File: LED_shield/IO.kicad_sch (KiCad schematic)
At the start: 69 parts, among them J201 Raspberry_Pi_2_3, Q201 PMOS, Q202 NMOS, Q203 NMOS, Q204 NMOS, Q205 NMOS, SW201 SW_DIP_x08, SW202 SW_DIP_x08, U201 7414, U202 7414, U203 4052

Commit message: Finish most of PCB design
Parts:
- added C204, C205, C206: 100n, Capacitor_SMD:C_0402_1005Metric, symbol Device:C
- R201, R202, R203: footprint Resistor_SMD:R_0603_1608Metric -> Resistor_SMD:R_0402_1005Metric; LCSC (none) -> C11702
- R204: renamed from R209; LCSC (none) -> C22797
- R205: renamed from R210; footprint Resistor_SMD:R_0603_1608Metric -> Resistor_SMD:R_0402_1005Metric; LCSC (none) -> C11702
- R206: renamed from R211; footprint Resistor_SMD:R_0603_1608Metric -> Resistor_SMD:R_0402_1005Metric; LCSC (none) -> C11702
- R207: renamed from R212; footprint Resistor_SMD:R_0603_1608Metric -> Resistor_SMD:R_0402_1005Metric; LCSC (none) -> C11702
- R209: renamed from R213; footprint Resistor_SMD:R_0603_1608Metric -> Resistor_SMD:R_0402_1005Metric; LCSC (none) -> C11702
- R210: renamed from R214; footprint Resistor_SMD:R_0603_1608Metric -> Resistor_SMD:R_0402_1005Metric; LCSC (none) -> C11702
- R211: renamed from R206; footprint Resistor_SMD:R_0603_1608Metric -> Resistor_SMD:R_0402_1005Metric; LCSC (none) -> C25744
- R212: renamed from R205; footprint Resistor_SMD:R_0603_1608Metric -> Resistor_SMD:R_0402_1005Metric; LCSC (none) -> C25744
- R213: renamed from R207; footprint Resistor_SMD:R_0603_1608Metric -> Resistor_SMD:R_0402_1005Metric; LCSC (none) -> C25744
- R214: renamed from R208; footprint Resistor_SMD:R_0603_1608Metric -> Resistor_SMD:R_0402_1005Metric; LCSC (none) -> C25744
- renumbered R204 to R208, R223 to R218, R221 to R219, R222 to R220, R224 to R221, R225 to R222, R227 to R223, R228 to R224, R226 to R225, R218 to R226, R219 to R227, R220 to R228, R235 to R232, R232 to R233, R233 to R234, R234 to R235, U203 to U201, U201 to U203
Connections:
- net +5V: now also C204.1, C205.1
- net 3V3: now also C206.1
- net ADC_{0}MCU: now also C201.1, R204.2, R205.1, U201.12 (X0)
- net ADC_{1}MCU: now also C203.1, R209.2, R210.1, U201.14 (X1)
- net GND: now also C204.2, C205.2, C206.2
- net LED0_MCU: now also A202.20 (GPIO15), U202.5; no longer A202.1 (GPIO0), U202.1
- net LED1_MCU: now also A202.19 (GPIO14); no longer A202.2 (GPIO1)
- net LED2_MCU: now also A202.15 (GPIO11), U202.1; no longer A202.4 (GPIO2), U202.5
- net LED3_MCU: now also A202.10 (GPIO7), U203.5; no longer A202.5 (GPIO3), U202.9
- net LED4_MCU: now also A202.9 (GPIO6), U203.3; no longer A202.21 (GPIO16), U203.11
- net LED5_MCU: now also A202.7 (GPIO5), U203.1; no longer A202.22 (GPIO17), U203.13
- net LED_OUT_0: now also U202.8; no longer U203.2
- net LED_OUT_1: now also U202.10; no longer U203.4
- net LED_OUT_2: now also U202.12; no longer U203.6
- net LED_OUT_4: now also U203.10; no longer U202.10
- net LED_OUT_5: now also U203.12; no longer U202.12
- net btn_read1: now also A202.21 (GPIO16); no longer A202.15 (GPIO11)
- net btn_read2: now also A202.24 (GPIO18); no longer A202.19 (GPIO14)
- net btn_read3: now also A202.22 (GPIO17); no longer A202.20 (GPIO15)
- net btn_sel0: now also A202.29 (GPIO22); no longer A202.6 (GPIO4)
- net btn_sel1: now also A202.25 (GPIO19); no longer A202.7 (GPIO5)
- net btn_sel2: now also A202.26 (GPIO20); no longer A202.9 (GPIO6)
- net btn_sel3: now also A202.27 (GPIO21); no longer A202.10 (GPIO7)
- net at U202.2: now also U202.13; no longer U203.1
- net at U203.9: now also U203.6; no longer U202.8
- net at U202.11: now also U202.4; no longer U203.10
- net at U202.6: now also U202.9; no longer U203.5
- new net: U203.13, U203.2
- new net: U203.11, U203.4
- no-connect marks 6 -> 42
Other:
- moved on the sheet: U202A, U202C, U202D, U202E, U202F, U203A, U203B, U203C, U203E, U203F

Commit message: Remove unused components
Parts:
- removed A201: Arduino_Nano_ESP32_Socket, PCM_arduino-library:Arduino_Nano_ESP32_Socket, symbol PCM_arduino-library:Arduino_Nano_ESP32_Socket
- removed C202, C206: 100n, Capacitor_SMD:C_0402_1005Metric, symbol Device:C
- removed D201: D_Schottky, symbol Device:D_Schottky
- removed J201: Raspberry_Pi_2_3, Connector_PinSocket_2.54mm:PinSocket_2x17_P2.54mm_Vertical, symbol Connector:Raspberry_Pi_2_3
- removed R201, R206, R207: 1k, Resistor_SMD:R_0402_1005Metric, symbol Device:R_US
- removed R215, R216, R217, R218, R219, R220, R221, R222, R223, R224, R225, R226, R227, R228, R229, R230, R231, R232, R233, R234, R235, R236: 0R, Resistor_SMD:R_0402_1005Metric, symbol Device:R_US
- removed U201: 4052, Package_SO:SO-16_3.9x9.9mm_P1.27mm, symbol 4xxx:4052
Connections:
- net 12VIN renamed VIN
- no-connect marks 42 -> 16
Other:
- note added: "7414 decoupling"
- note added: "MCU module"
- note added: "Output buffering"
- note added: "Voltage dividers for rail monitoring"
- note added: "dip switch matrix"
- moved on the sheet: A202, C201, C203, C204, C205, D202, D203, D204, D205, D206, D207, D208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

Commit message: Small fixes before production
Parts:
- removed D202, D203, D204, D205, D206, D207, D208, D209, D210, D211, D212, D213, D214, D215, D216, D217: D_Small_Filled, Diode_SMD:D_0603_1608Metric, symbol Device:D_Small_Filled
- removed Q202, Q203, Q204, Q205: NMOS, Package_TO_SOT_SMD:SOT-23, symbol Simulation_SPICE:NMOS
- added C202, C206: 100n, Capacitor_SMD:C_0402_1005Metric, symbol Device:C
- added R201, R206, R207, R215, R216, R217, R218, R219, R220, R221, R222, R223: 100k, Resistor_SMD:R_0402_1005Metric, symbol Device:R_US
- added U201, U204: 74HC165, Package_SO:SOIC-16_3.9x9.9mm_P1.27mm, symbol 74xx:74HC165
- Q201: symbol Simulation_SPICE:PMOS -> Device:Q_PMOS_GSD; LCSC (none) -> C10487
- R211, R212, R213, R214: value 10k -> 100k; LCSC C25744 -> C25741
- SW201, SW202: footprint Button_Switch_SMD:SW_DIP_SPSTx08_Slide_6.7x21.88mm_W6.73mm_P2.54mm_LowProfile_JPin -> Button_Switch_SMD:SW_DIP_SPSTx08_Slide_6.7x21.88mm_W8.61mm_P2.54mm_LowProfile
- U202, U203: LCSC (none) -> C5605
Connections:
- net +5V: now also Q201.3 (D); no longer Q201.1 (D)
- net 3V3: now also SW201.10, SW201.11, SW201.12, SW201.13, SW201.14, SW201.15, SW201.16, SW201.9, SW202.1, SW202.2, SW202.3, SW202.4, SW202.5, SW202.6, SW202.7, SW202.8, C202.1, C206.1, U201.16 (VCC), U204.16 (VCC); no longer R211.2, R212.2, R213.2, R214.2
- net 5V_local: now also Q201.2 (S); no longer Q201.3 (S)
- net GND: now also R211.2, R212.2, R213.2, R214.2, C202.2, C206.2, R201.2, R206.2, R207.2, R215.2, R216.2, R217.2, R218.2, R219.2, R220.2, R221.2, R222.2, R223.2, U201.8 (GND), U204.8 (GND)
- net btn_read0: no longer SW201.13, SW201.14, SW201.15, SW201.16
- net at SW201.7: now also R206.1, U204.5 (D6)
- net at R213.1: now also SW201.3, U204.13 (D2)
- net at R211.1: now also SW201.5, U204.3 (D4)
- net at R212.1: now also SW201.4, U204.14 (D3)
- net at SW201.2: now also R214.1, U204.12 (D1)
- net at SW201.8: now also R201.1, U204.6 (D7)
- net at R202.2, R203.2: now also Q201.1 (G); no longer Q201.2 (G)
- net at SW201.1: now also R215.1, U204.11 (D0)
- net at SW201.6: now also R207.1, U204.4 (D5)
- removed net btn_read1: A202.21 (GPIO16), SW201.10, SW201.11, SW201.12, SW201.9
- removed net btn_read2: A202.24 (GPIO18), SW202.13, SW202.14, SW202.15, SW202.16
- removed net btn_read3: A202.22 (GPIO17), SW202.10, SW202.11, SW202.12, SW202.9
- net btn_sel0: no longer names the net of A202.29 (GPIO22)
- net btn_sel1 renamed ~{PL}
- net ~{PL}: now also U201.1 (~{PL}), U204.1 (~{PL})
- net btn_sel2 renamed ~{CE}
- net ~{CE}: now also U201.15 (~{CE}), U204.15 (~{CE})
- net btn_sel3: no longer names the net of A202.27 (GPIO21)
- new net: U201.10 (DS), U204.9 (Q7)
- new net: R220.1, SW202.13, U201.14 (D3)
- new net: R222.1, SW202.15, U201.12 (D1)
- new net: R216.1, SW202.9, U201.6 (D7)
- new net: R217.1, SW202.10, U201.5 (D6)
- new net: R218.1, SW202.11, U201.4 (D5)
- new net: R219.1, SW202.12, U201.3 (D4)
- new net: R221.1, SW202.14, U201.13 (D2)
- new net: R223.1, SW202.16, U201.11 (D0)
- new net CP: A202.24 (GPIO18), U201.2 (CP), U204.2 (CP)
- new net Ser_in: A202.21 (GPIO16), U201.9 (Q7)
- no-connect marks 16 -> 19
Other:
- note added: "74165 decoupling"
- moved on the sheet: C204, C205, SW201, SW202

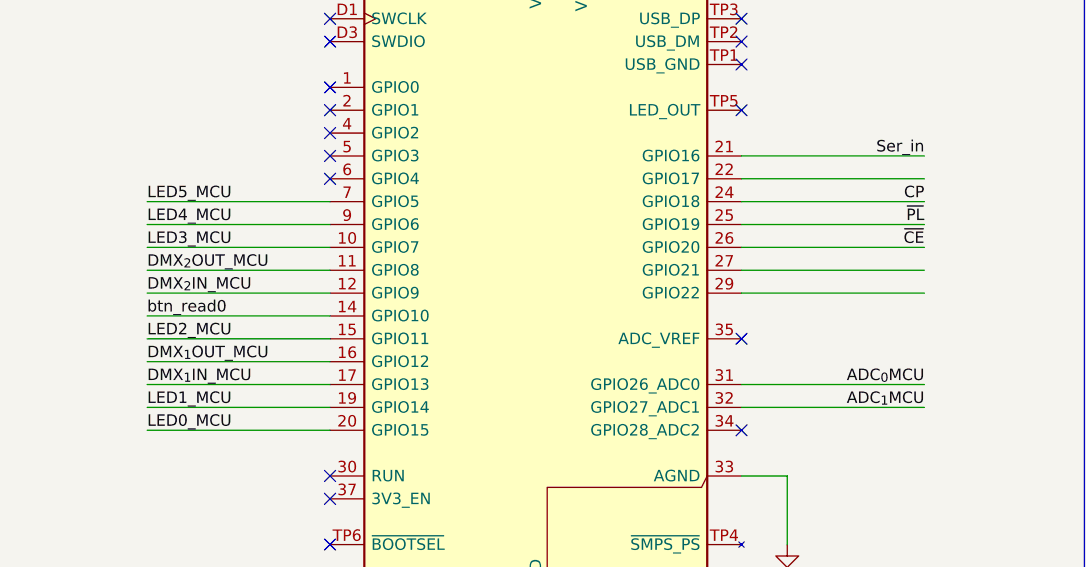
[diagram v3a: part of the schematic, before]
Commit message: Make PCB ready for manufacture (again)
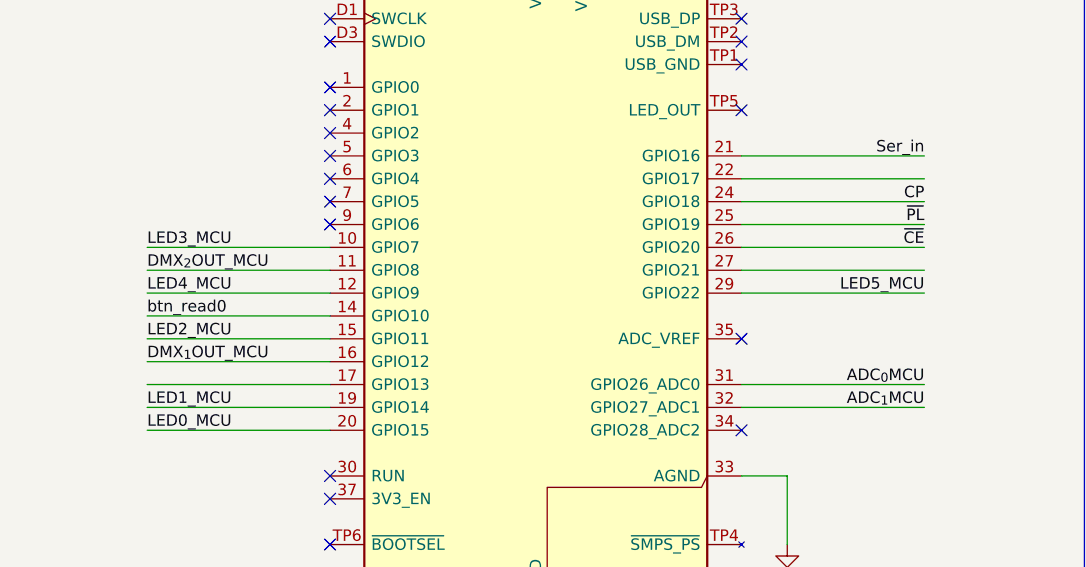
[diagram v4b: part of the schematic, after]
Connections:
- net DMX_{2}IN_MCU is gone; now on net LED4_MCU: A202.12 (GPIO9)
- net LED4_MCU: no longer A202.9 (GPIO6)
- net LED5_MCU: now also A202.29 (GPIO22); no longer A202.7 (GPIO5)
- net DMX_{1}IN_MCU: no longer names the net of A202.17 (GPIO13)
- no-connect marks 19 -> 21

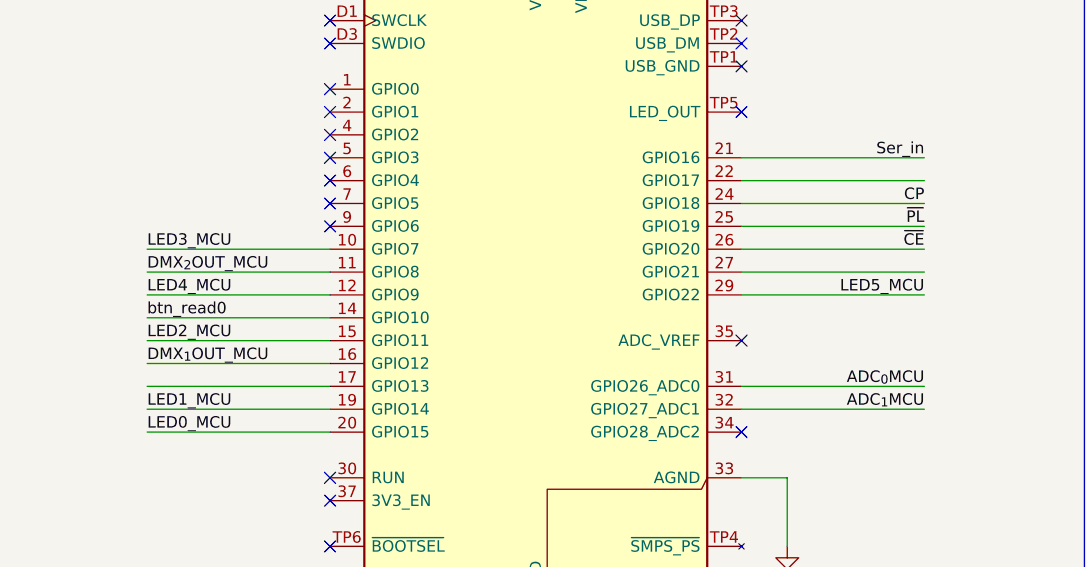
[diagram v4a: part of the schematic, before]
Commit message: Add missing LCSC partnumbers
Also fixed grouping in PCB
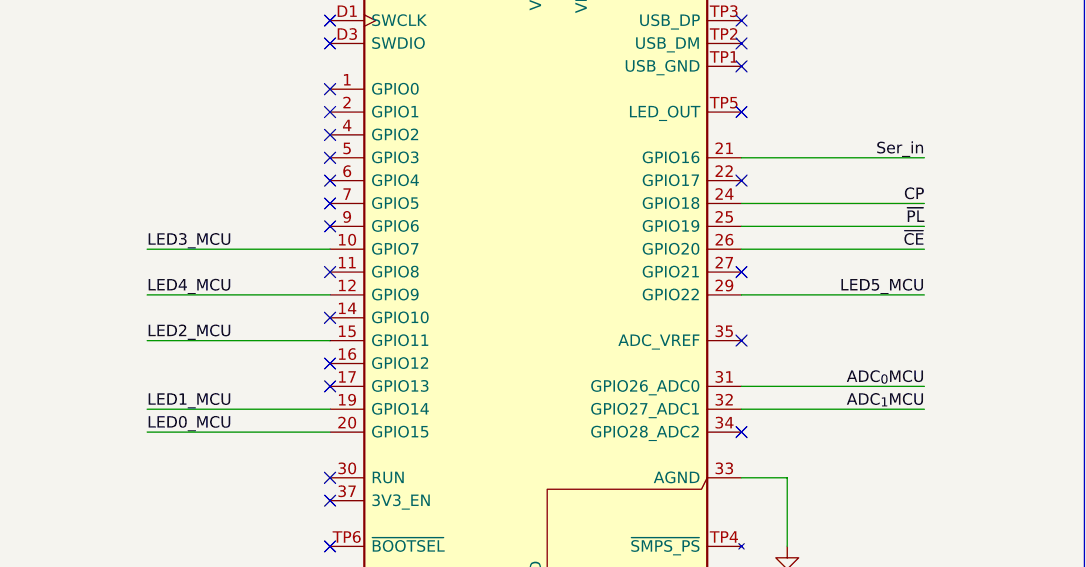
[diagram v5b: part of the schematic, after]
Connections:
- net DMX_{1}OUT_MCU: no longer names the net of A202.16 (GPIO12)
- net DMX_{2}OUT_MCU: no longer names the net of A202.11 (GPIO8)
- net btn_read0: no longer names the net of A202.14 (GPIO10)
- no-connect marks 21 -> 27
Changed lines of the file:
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@@
+	)
+	(no_connect
+		(at 43.18 236.22)
+	)
+	(no_connect
+		(at 43.18 223.52)
 	)
 	(no_connect
@@
 	)
 	(no_connect
+		(at 88.9 213.36)
+	)
+	(no_connect
 		(at 43.18 246.38)
+	)
+	(no_connect
+		(at 88.9 223.52)
 	)
 	(no_connect
@@
 	)
 	(no_connect
+		(at 43.18 233.68)
+	)
+	(no_connect
 		(at 43.18 215.9)
+	)
+	(no_connect
+		(at 43.18 228.6)
 	)
 	(no_connect
@@
 	(wire
 		(pts
-			(xy 22.86 228.6) (xy 43.18 228.6)
-		)
-		(stroke
-			(width 0)
-			(type default)
-		)
-	)
-	(wire
-		(pts
 			(xy 165.1 152.4) (xy 170.18 152.4)
 		)
@@
 	(wire
 		(pts
-			(xy 109.22 213.36) (xy 88.9 213.36)
-		)
-		(stroke
-			(width 0)
-			(type default)
-		)
-	)
-	(wire
-		(pts
 			(xy 160.02 226.06) (xy 165.1 226.06)
 		)
@@
 	(wire
 		(pts
-			(xy 22.86 233.68) (xy 43.18 233.68)
-		)
-		(stroke
-			(width 0)
-			(type default)
-		)
-	)
-	(wire
-		(pts
 			(xy 109.22 218.44) (xy 88.9 218.44)
 		)
@@
 	(wire
 		(pts
-			(xy 109.22 223.52) (xy 88.9 223.52)
-		)
-		(stroke
-			(width 0)
-			(type default)
-		)
-	)
-	(wire
-		(pts
 			(xy 185.42 119.38) (xy 185.42 142.24)
 		)
@@
 	(wire
 		(pts
-			(xy 22.86 223.52) (xy 43.18 223.52)
-		)
-		(stroke
-			(width 0)
-			(type default)
-		)
-	)
-	(wire
-		(pts
 			(xy 190.5 226.06) (xy 195.58 226.06)
 		)
@@
 		(pts
 			(xy 134.62 205.74) (xy 142.24 205.74)
-		)
-		(stroke
-			(width 0)
-			(type default)
-		)
-	)
-	(wire
-		(pts
-			(xy 22.86 236.22) (xy 43.18 236.22)
 		)
 		(stroke
@@
 		)
 	)
-	(label "DMX_{1}OUT_MCU"
-		(at 22.86 233.68 0)
-		(fields_autoplaced yes)
-		(effects
-			(font
-				(size 1.27 1.27)
-			)
-			(justify left bottom)
-		)
-	)
 	(label "CP"
 		(at 203.2 215.9 0)
@@
 		)
 	)
-	(label "DMX_{2}OUT_MCU"
-		(at 22.86 223.52 0)
-		(fields_autoplaced yes)
-		(effects
-			(font
-				(size 1.27 1.27)
-			)
-			(justify left bottom)
-		)
-	)
 	(label "LED0_MCU"
 		(at 287.02 71.12 0)
@@
 		)
 	)
-	(label "btn_read0"
-		(at 22.86 228.6 0)
-		(fields_autoplaced yes)
-		(effects
-			(font
-				(size 1.27 1.27)
-			)
-			(justify left bottom)
-		)
-	)
